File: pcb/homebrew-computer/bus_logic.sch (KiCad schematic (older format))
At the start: 11 parts

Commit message: Keep working on the peripheral interface
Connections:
- net BRIDGE renamed BRIDGE_I
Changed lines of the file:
@@
 	1450 3050 1450 3150
 Text HLabel 2150 3100 2    50   Input ~ 0
-BRIDGE
+BRIDGE_I
 Text HLabel 1450 3100 0    50   Input ~ 0
 A_TO_D
 $Comp
-L power:GND #PWR?
+L power:GND #PWR0121
 U 1 1 5F90DF37
 P 3150 2150
-F 0 "#PWR?" H 3150 1900 50  0001 C CNN
+F 0 "#PWR0121" H 3150 1900 50  0001 C CNN
 F 1 "GND" H 3155 1977 50  0000 C CNN
 F 2 "" H 3150 2150 50  0001 C CNN
@@
 	3150 2000 3150 1900
 $Comp
-L power:GND #PWR?
+L power:GND #PWR0122
 U 1 1 5F90E759
 P 1000 1650
-F 0 "#PWR?" H 1000 1400 50  0001 C CNN
+F 0 "#PWR0122" H 1000 1400 50  0001 C CNN
 F 1 "GND" H 1005 1477 50  0000 C CNN
 F 2 "" H 1000 1650 50  0001 C CNN
@@
 Connection ~ 1000 1650
 $Comp
-L power:+3.3V #PWR?
+L power:+3.3V #PWR0123
 U 1 1 5F911BCD
 P 1000 1450
-F 0 "#PWR?" H 1000 1300 50  0001 C CNN
+F 0 "#PWR0123" H 1000 1300 50  0001 C CNN
 F 1 "+3.3V" H 1015 1623 50  0000 C CNN
 F 2 "" H 1000 1450 50  0001 C CNN
@@
 	1600 1650 1900 1650
 $Comp
-L power:+3.3V #PWR?
+L power:+3.3V #PWR0124
 U 1 1 5F913D52
 P 2400 1500
-F 0 "#PWR?" H 2400 1350 50  0001 C CNN
+F 0 "#PWR0124" H 2400 1350 50  0001 C CNN
 F 1 "+3.3V" H 2250 1650 50  0000 C CNN
 F 2 "" H 2400 1500 50  0001 C CNN
@@
 DBUS2
 $Comp
-L power:GND #PWR?
+L power:GND #PWR0125
 U 1 1 5F947DF0
 P 6500 3600
-F 0 "#PWR?" H 6500 3350 50  0001 C CNN
+F 0 "#PWR0125" H 6500 3350 50  0001 C CNN
 F 1 "GND" H 6505 3427 50  0000 C CNN
 F 2 "" H 6500 3600 50  0001 C CNN
@@
 ABUS2
 $Comp
-L power:GND #PWR?
+L power:GND #PWR0126
 U 1 1 5F948EED
 P 7600 3600
-F 0 "#PWR?" H 7600 3350 50  0001 C CNN
+F 0 "#PWR0126" H 7600 3350 50  0001 C CNN
 F 1 "GND" H 7605 3427 50  0000 C CNN
 F 2 "" H 7600 3600 50  0001 C CNN

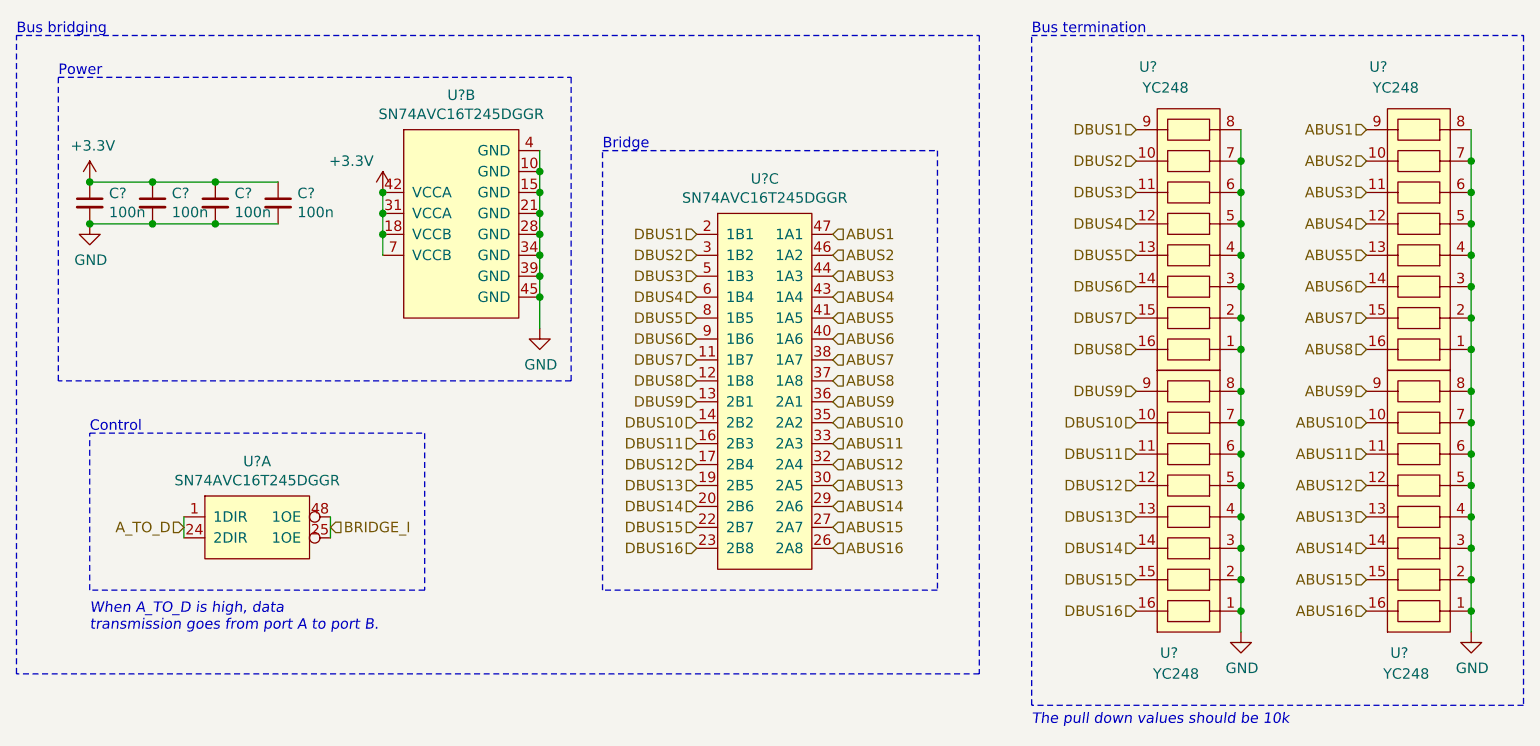
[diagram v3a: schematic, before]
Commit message: Remove the address bus as it would require too big of a connector
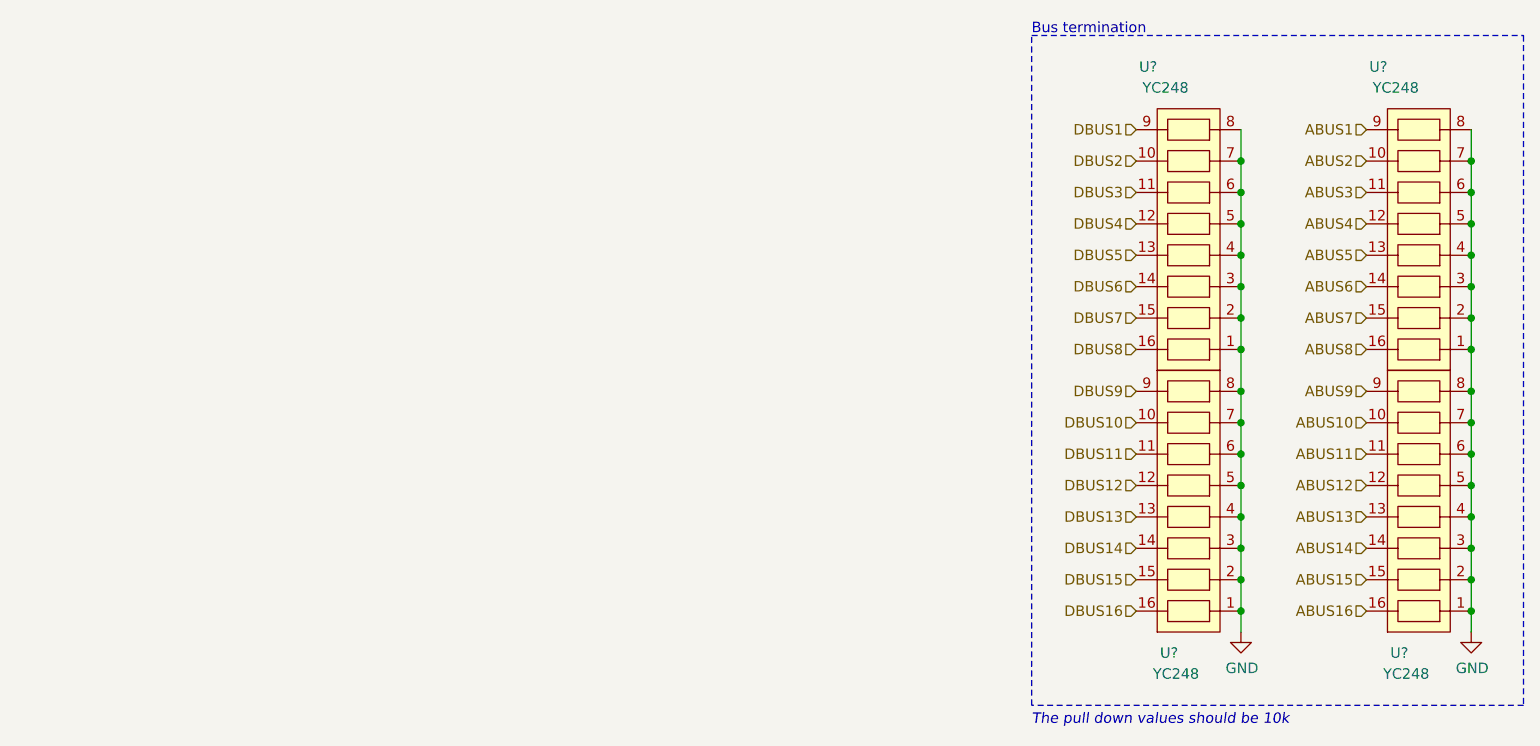
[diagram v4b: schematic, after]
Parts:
- removed C? (x4): 100n, symbol Device:C_Small
- removed U? (x3): SN74AVC16T245DGGR, symbol 74AVC16T245:SN74AVC16T245DGGR
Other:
- note removed: "Bridge"
- note removed: "Bus bridging"
- note removed: "Control"
- note removed: "Power"
- note removed: "When A_TO_D is high, data \ntransmission goes from port A to port B."
